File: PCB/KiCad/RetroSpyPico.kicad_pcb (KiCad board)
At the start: 2 copper layers, 48.3 x 83.4 mm, 18 parts, among them CN1 Conn_02x05_Row_Letter_First, CN2 Conn_02x05_Row_Letter_First, SW1 SW_SPDT, SW2 SW_Push, U1 Raspberry Pi Pico

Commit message: add JLCJLCJLCJLC
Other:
- board text added: "JLCJLCJLCJLC"
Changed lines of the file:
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@@
   (gr_line (start 150.495 39.1922) (end 121.285 39.1922) (layer "Edge.Cuts") (width 0.1))
   (gr_line (start 160.02 50.165) (end 156.21 50.165) (layer "Edge.Cuts") (width 0.1))
+  (gr_text "JLCJLCJLCJLC" (at 135.89 119.38) (layer "B.SilkS")
+    (effects (font (size 1 1) (thickness 0.15)) (justify mirror))
+  )
   (gr_text "DATA" (at 125.73 96.52) (layer "F.SilkS")
     (effects (font (size 0.8 0.8) (thickness 0.15)))

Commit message: update KiCad
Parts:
- REF** (x4): footprint MountingHole:MountingHole_3.2mm_M3 -> Library:MountingHole_3.2mm_M3

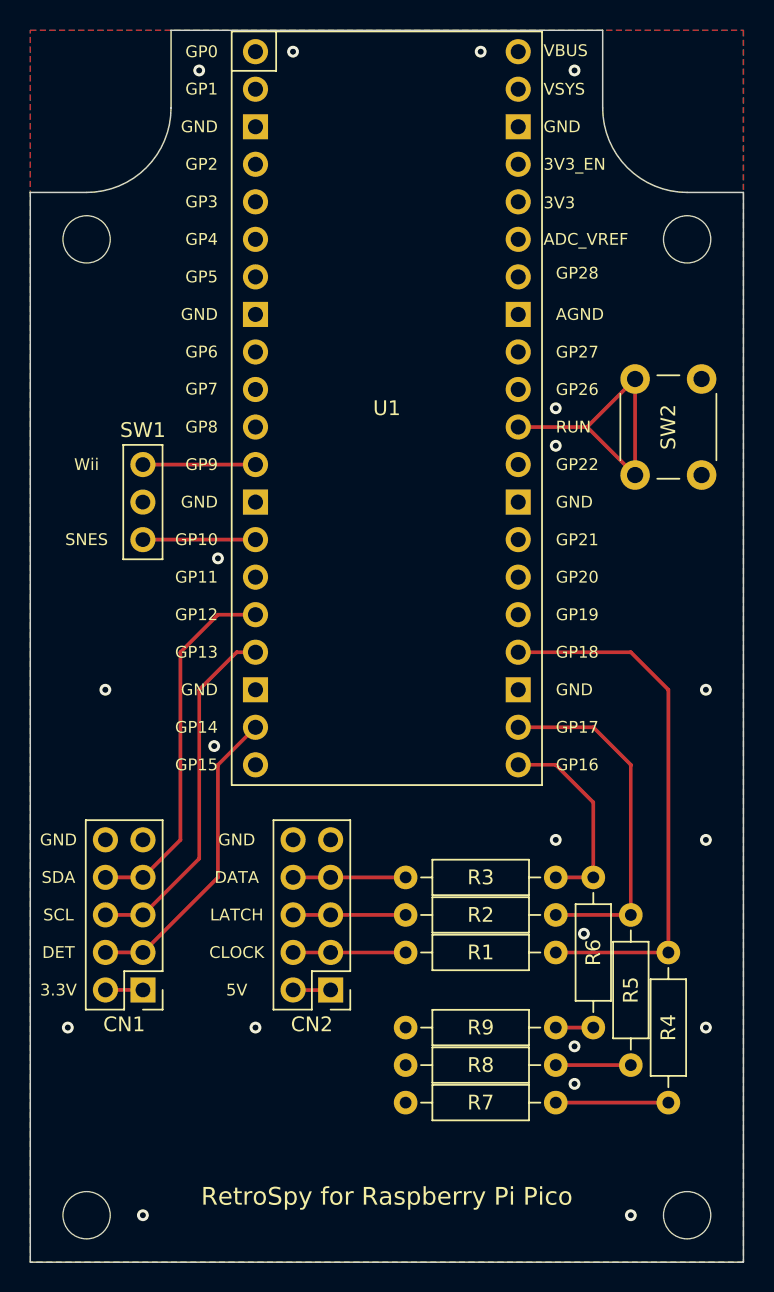
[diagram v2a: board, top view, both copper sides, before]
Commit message: Allows Raspberry Pi Pico to be soldered directly to the board without pin headers.
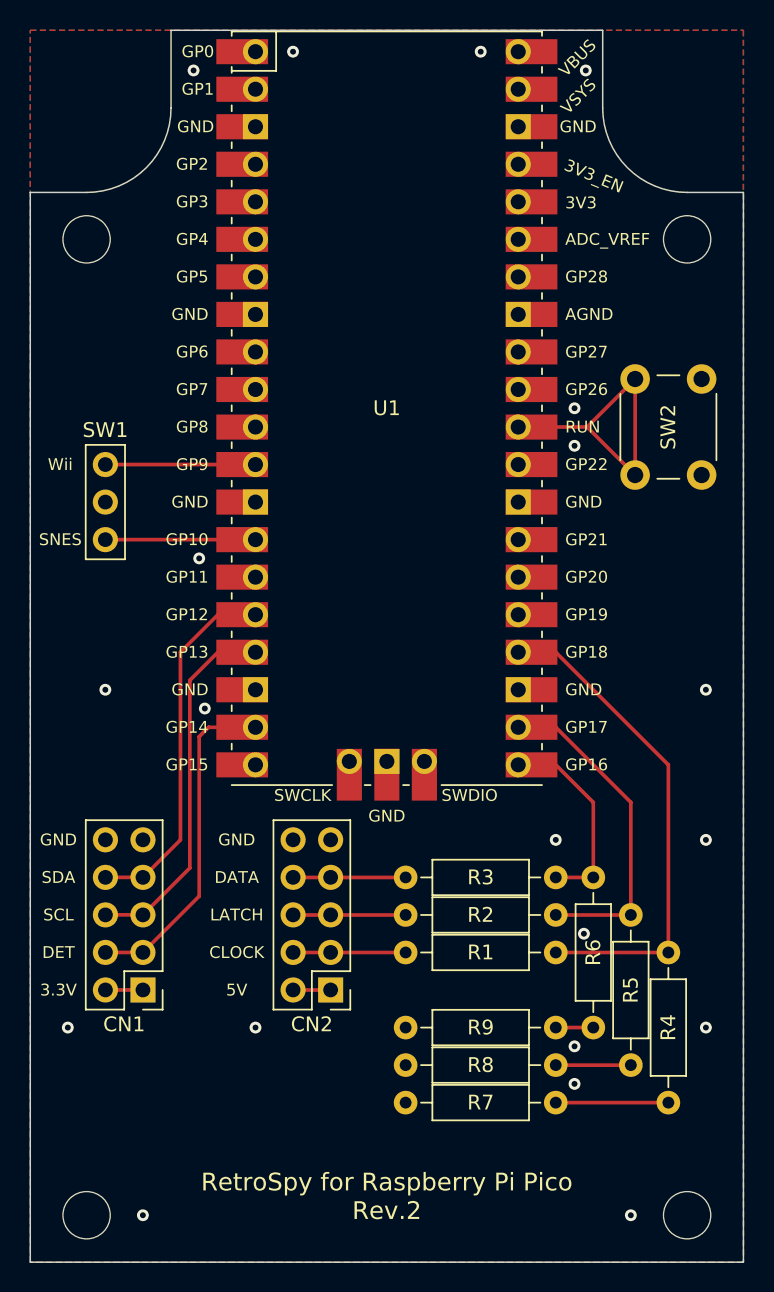
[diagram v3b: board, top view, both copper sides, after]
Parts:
- moved SW1 2.54 mm to (116.8, 68.6)
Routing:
- net Net-(U1-GPIO18): track 36.6 -> 33.6 mm
- net Net-(SW1-C): track 7.62 -> 10.2 mm
- net Net-(SW1-A): track 7.62 -> 10.2 mm
- net Net-(CN1-Pin_3): track 20.9 -> 22.8 mm
- net Net-(U1-GPIO17): track 23.9 -> 22.4 mm
- net Net-(CN1-Pin_5): track 24.2 -> 25.0 mm
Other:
- board text added: "RetroSpy for Raspberry Pi Pico Rev.2"
- board text removed: "RetroSpy for Raspberry Pi Pico"
